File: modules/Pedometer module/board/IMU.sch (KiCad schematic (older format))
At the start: 6 parts, among them J4 Conn_01x08_Female, U3 ADXL345BCCZ

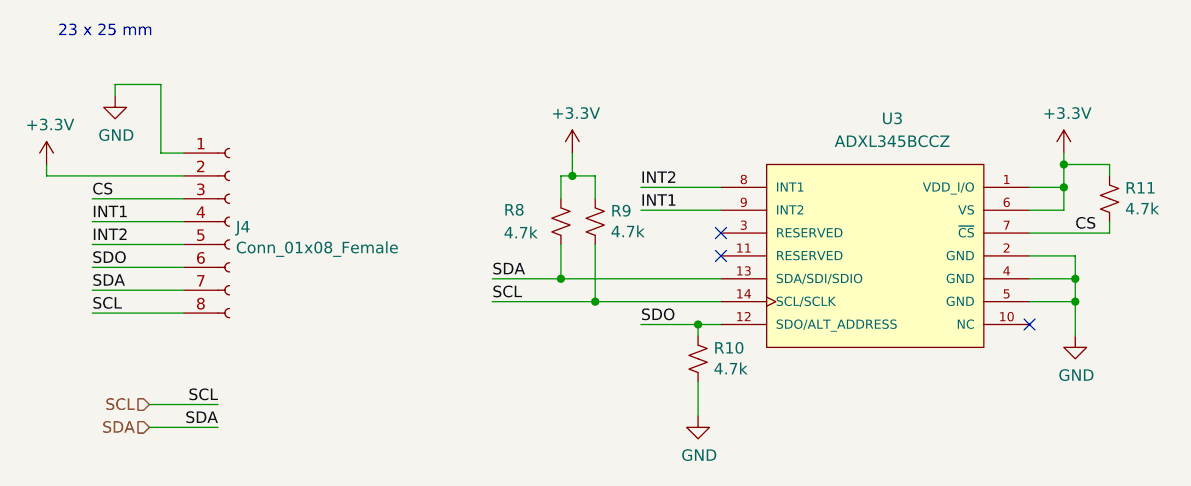
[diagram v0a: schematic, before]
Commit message: Pedometer module: Schematic and PCB layout
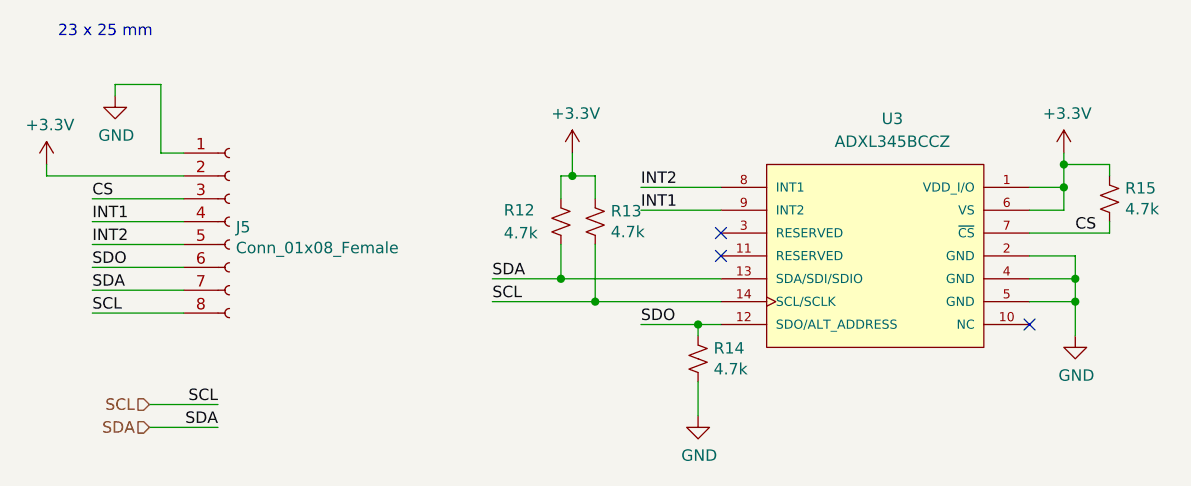
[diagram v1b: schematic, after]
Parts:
- J5: renamed from J4; footprint Connector_PinSocket_2.54mm:PinSocket_1x08_P2.54mm_Vertical -> Board:ADXL345_Breakout
- renumbered R8 to R12, R9 to R13, R10 to R14, R11 to R15
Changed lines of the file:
@@
 SCL
 $Comp
-L Connector:Conn_01x08_Female J4
+L Connector:Conn_01x08_Female J5
 U 1 1 61A32798
 P 4200 3250
-F 0 "J4" H 4228 3226 50  0000 L CNN
+F 0 "J5" H 4228 3226 50  0000 L CNN
 F 1 "Conn_01x08_Female" H 4228 3135 50  0000 L CNN
-F 2 "Connector_PinSocket_2.54mm:PinSocket_1x08_P2.54mm_Vertical" H 4200 3250 50  0001 C CNN
+F 2 "Board:ADXL345_Breakout" H 4200 3250 50  0001 C CNN
 F 3 "~" H 4200 3250 50  0001 C CNN
 	1    4200 3250
@@
 	3700 2650 3700 2700
 $Comp
-L power:+3.3V #PWR024
+L power:+3.3V #PWR022
 U 1 1 61A36F21
 P 3400 3000
-F 0 "#PWR024" H 3400 2850 50  0001 C CNN
+F 0 "#PWR022" H 3400 2850 50  0001 C CNN
 F 1 "+3.3V" H 3415 3173 50  0000 C CNN
 F 2 "" H 3400 3000 50  0001 C CNN
@@
 $EndComp
 $Comp
-L power:GND #PWR025
+L power:GND #PWR023
 U 1 1 61A37647
 P 3700 2700
-F 0 "#PWR025" H 3700 2450 50  0001 C CNN
+F 0 "#PWR023" H 3700 2450 50  0001 C CNN
 F 1 "GND" H 3705 2527 50  0000 C CNN
 F 2 "" H 3700 2700 50  0001 C CNN
@@
 INT2
 $Comp
-L power:GND #PWR029
+L power:GND #PWR027
 U 1 1 619B5978
 P 7900 3750
-F 0 "#PWR029" H 7900 3500 50  0001 C CNN
+F 0 "#PWR027" H 7900 3500 50  0001 C CNN
 F 1 "GND" H 7905 3577 50  0000 C CNN
 F 2 "" H 7900 3750 50  0001 C CNN
@@
 $EndComp
 $Comp
-L power:+3.3V #PWR028
+L power:+3.3V #PWR026
 U 1 1 619B5CC3
 P 7850 2950
-F 0 "#PWR028" H 7850 2800 50  0001 C CNN
+F 0 "#PWR026" H 7850 2800 50  0001 C CNN
 F 1 "+3.3V" H 7865 3123 50  0000 C CNN
 F 2 "" H 7850 2950 50  0001 C CNN
@@
 	7850 3000 7850 2950
 $Comp
-L Device:R_Small_US R11
+L Device:R_Small_US R15
 U 1 1 619BA566
 P 8050 3150
-F 0 "R11" H 8118 3196 50  0000 L CNN
+F 0 "R15" H 8118 3196 50  0000 L CNN
 F 1 "4.7k" H 8118 3105 50  0000 L CNN
 F 2 "Resistor_SMD:R_0805_2012Metric_Pad1.20x1.40mm_HandSolder" H 8050 3150 50  0001 C CNN
@@
 	5350 3600 5800 3600
 $Comp
-L Device:R_Small_US R9
+L Device:R_Small_US R13
 U 1 1 619BEF64
 P 5800 3250
-F 0 "R9" H 5868 3296 50  0000 L CNN
+F 0 "R13" H 5868 3296 50  0000 L CNN
 F 1 "4.7k" H 5868 3205 50  0000 L CNN
 F 2 "Resistor_SMD:R_0805_2012Metric_Pad1.20x1.40mm_HandSolder" H 5800 3250 50  0001 C CNN
@@
 $EndComp
 $Comp
-L Device:R_Small_US R8
+L Device:R_Small_US R12
 U 1 1 619BF83C
 P 5650 3250
-F 0 "R8" H 5400 3300 50  0000 L CNN
+F 0 "R12" H 5400 3300 50  0000 L CNN
 F 1 "4.7k" H 5400 3200 50  0000 L CNN
 F 2 "Resistor_SMD:R_0805_2012Metric_Pad1.20x1.40mm_HandSolder" H 5650 3250 50  0001 C CNN
@@
 	5700 3050 5800 3050
 $Comp
-L power:+3.3V #PWR026
+L power:+3.3V #PWR024
 U 1 1 619C4436
 P 5700 2950
-F 0 "#PWR026" H 5700 2800 50  0001 C CNN
+F 0 "#PWR024" H 5700 2800 50  0001 C CNN
 F 1 "+3.3V" H 5715 3123 50  0000 C CNN
 F 2 "" H 5700 2950 50  0001 C CNN
@@
 $EndComp
 $Comp
-L Device:R_Small_US R10
+L Device:R_Small_US R14
 U 1 1 619CBE84
 P 6250 3850
-F 0 "R10" H 6318 3896 50  0000 L CNN
+F 0 "R14" H 6318 3896 50  0000 L CNN
 F 1 "4.7k" H 6318 3805 50  0000 L CNN
 F 2 "Resistor_SMD:R_0805_2012Metric_Pad1.20x1.40mm_HandSolder" H 6250 3850 50  0001 C CNN
@@
 	6250 3700 6000 3700
 $Comp
-L power:GND #PWR027
+L power:GND #PWR025
 U 1 1 619CD6B6
 P 6250 4100
-F 0 "#PWR027" H 6250 3850 50  0001 C CNN
+F 0 "#PWR025" H 6250 3850 50  0001 C CNN
 F 1 "GND" H 6255 3927 50  0000 C CNN
 F 2 "" H 6250 4100 50  0001 C CNN

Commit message: Pedometer module: PCB size reduced
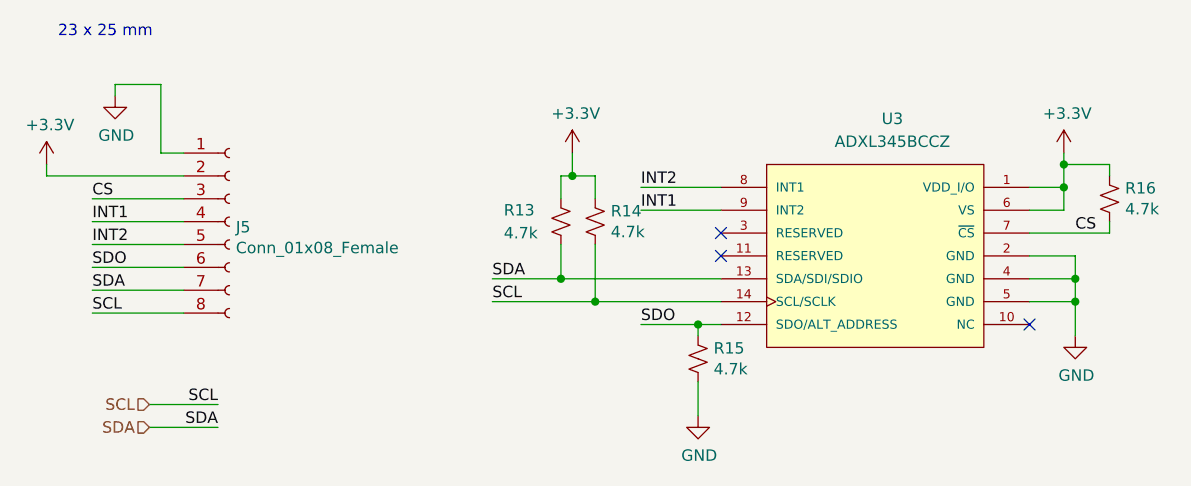
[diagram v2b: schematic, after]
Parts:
- renumbered R12 to R13, R13 to R14, R14 to R15, R15 to R16
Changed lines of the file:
@@
 	3700 2650 3700 2700
 $Comp
-L power:+3.3V #PWR022
+L power:+3.3V #PWR023
 U 1 1 61A36F21
 P 3400 3000
-F 0 "#PWR022" H 3400 2850 50  0001 C CNN
+F 0 "#PWR023" H 3400 2850 50  0001 C CNN
 F 1 "+3.3V" H 3415 3173 50  0000 C CNN
 F 2 "" H 3400 3000 50  0001 C CNN
@@
 $EndComp
 $Comp
-L power:GND #PWR023
+L power:GND #PWR024
 U 1 1 61A37647
 P 3700 2700
-F 0 "#PWR023" H 3700 2450 50  0001 C CNN
+F 0 "#PWR024" H 3700 2450 50  0001 C CNN
 F 1 "GND" H 3705 2527 50  0000 C CNN
 F 2 "" H 3700 2700 50  0001 C CNN
@@
 INT2
 $Comp
-L power:GND #PWR027
+L power:GND #PWR028
 U 1 1 619B5978
 P 7900 3750
-F 0 "#PWR027" H 7900 3500 50  0001 C CNN
+F 0 "#PWR028" H 7900 3500 50  0001 C CNN
 F 1 "GND" H 7905 3577 50  0000 C CNN
 F 2 "" H 7900 3750 50  0001 C CNN
@@
 $EndComp
 $Comp
-L power:+3.3V #PWR026
+L power:+3.3V #PWR027
 U 1 1 619B5CC3
 P 7850 2950
-F 0 "#PWR026" H 7850 2800 50  0001 C CNN
+F 0 "#PWR027" H 7850 2800 50  0001 C CNN
 F 1 "+3.3V" H 7865 3123 50  0000 C CNN
 F 2 "" H 7850 2950 50  0001 C CNN
@@
 	7850 3000 7850 2950
 $Comp
-L Device:R_Small_US R15
+L Device:R_Small_US R16
 U 1 1 619BA566
 P 8050 3150
-F 0 "R15" H 8118 3196 50  0000 L CNN
+F 0 "R16" H 8118 3196 50  0000 L CNN
 F 1 "4.7k" H 8118 3105 50  0000 L CNN
 F 2 "Resistor_SMD:R_0805_2012Metric_Pad1.20x1.40mm_HandSolder" H 8050 3150 50  0001 C CNN
@@
 	5350 3600 5800 3600
 $Comp
-L Device:R_Small_US R13
+L Device:R_Small_US R14
 U 1 1 619BEF64
 P 5800 3250
-F 0 "R13" H 5868 3296 50  0000 L CNN
+F 0 "R14" H 5868 3296 50  0000 L CNN
 F 1 "4.7k" H 5868 3205 50  0000 L CNN
 F 2 "Resistor_SMD:R_0805_2012Metric_Pad1.20x1.40mm_HandSolder" H 5800 3250 50  0001 C CNN
@@
 $EndComp
 $Comp
-L Device:R_Small_US R12
+L Device:R_Small_US R13
 U 1 1 619BF83C
 P 5650 3250
-F 0 "R12" H 5400 3300 50  0000 L CNN
+F 0 "R13" H 5400 3300 50  0000 L CNN
 F 1 "4.7k" H 5400 3200 50  0000 L CNN
 F 2 "Resistor_SMD:R_0805_2012Metric_Pad1.20x1.40mm_HandSolder" H 5650 3250 50  0001 C CNN
@@
 	5700 3050 5800 3050
 $Comp
-L power:+3.3V #PWR024
+L power:+3.3V #PWR025
 U 1 1 619C4436
 P 5700 2950
-F 0 "#PWR024" H 5700 2800 50  0001 C CNN
+F 0 "#PWR025" H 5700 2800 50  0001 C CNN
 F 1 "+3.3V" H 5715 3123 50  0000 C CNN
 F 2 "" H 5700 2950 50  0001 C CNN
@@
 $EndComp
 $Comp
-L Device:R_Small_US R14
+L Device:R_Small_US R15
 U 1 1 619CBE84
 P 6250 3850
-F 0 "R14" H 6318 3896 50  0000 L CNN
+F 0 "R15" H 6318 3896 50  0000 L CNN
 F 1 "4.7k" H 6318 3805 50  0000 L CNN
 F 2 "Resistor_SMD:R_0805_2012Metric_Pad1.20x1.40mm_HandSolder" H 6250 3850 50  0001 C CNN
@@
 	6250 3700 6000 3700
 $Comp
-L power:GND #PWR025
+L power:GND #PWR026
 U 1 1 619CD6B6
 P 6250 4100
-F 0 "#PWR025" H 6250 3850 50  0001 C CNN
+F 0 "#PWR026" H 6250 3850 50  0001 C CNN
 F 1 "GND" H 6255 3927 50  0000 C CNN
 F 2 "" H 6250 4100 50  0001 C CNN

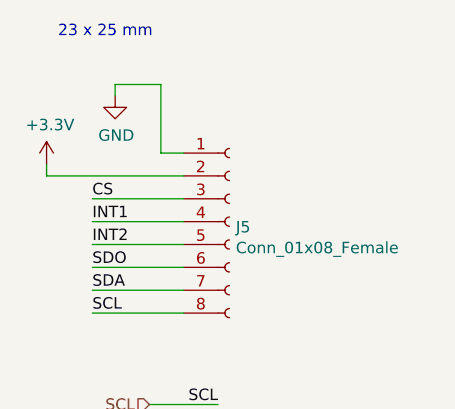
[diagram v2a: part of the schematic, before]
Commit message: Pedometer module: PCB complete
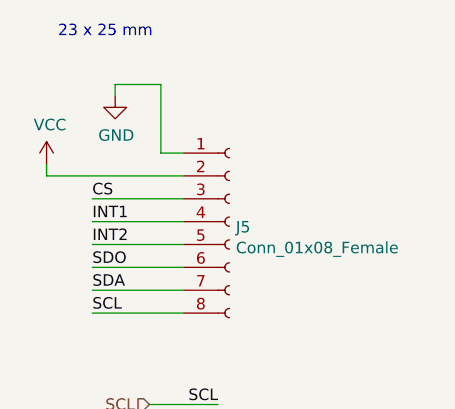
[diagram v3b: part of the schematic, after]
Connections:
- net +3V3: no longer J5.2 (Pin_2)
- new net VCC: J5.2 (Pin_2)
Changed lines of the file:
@@
 	3700 2650 3700 2700
-$Comp
-L power:+3.3V #PWR023
-U 1 1 61A36F21
-P 3400 3000
-F 0 "#PWR023" H 3400 2850 50  0001 C CNN
-F 1 "+3.3V" H 3415 3173 50  0000 C CNN
-F 2 "" H 3400 3000 50  0001 C CNN
-F 3 "" H 3400 3000 50  0001 C CNN
-	1    3400 3000
-	1    0    0    -1
-$EndComp
 $Comp
 L power:GND #PWR024
@@
 Text Label 7900 3300 0    50   ~ 0
 CS
+$Comp
+L power:VCC #PWR0101
+U 1 1 6247B16D
+P 3400 3000
+F 0 "#PWR0101" H 3400 2850 50  0001 C CNN
+F 1 "VCC" H 3415 3173 50  0000 C CNN
+F 2 "" H 3400 3000 50  0001 C CNN
+F 3 "" H 3400 3000 50  0001 C CNN
+	1    3400 3000
+	1    0    0    -1
+$EndComp
 $EndSCHEMATC
